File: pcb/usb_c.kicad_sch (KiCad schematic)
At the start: 6 parts, among them J5 USB_C_Receptacle_USB2.0_14P, U8 TPS2051CDBV, U9 USBLC6-2SC6

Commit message: pcb: satisfy ERC warnings and errors
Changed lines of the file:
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@@
+	)
+	(junction
+		(at 35.56 111.76)
+		(diameter 0)
+		(color 0 0 0 0)
 	)
 	(junction
@@
 	(wire
 		(pts
-			(xy 31.75 111.76) (xy 41.91 111.76)
+			(xy 31.75 111.76) (xy 35.56 111.76)
 		)
 		(stroke
@@
 		(pts
 			(xy 180.34 110.49) (xy 124.46 110.49)
+		)
+		(stroke
+			(width 0)
+			(type default)
+		)
+	)
+	(wire
+		(pts
+			(xy 35.56 111.76) (xy 41.91 111.76)
 		)
 		(stroke
@@
 					(unit 1)
 				)
+			)
+		)
+	)
+	(symbol
+		(lib_id "power:PWR_FLAG")
+		(at 35.56 111.76 0)
+		(unit 1)
+		(body_style 1)
+		(exclude_from_sim no)
+		(in_bom yes)
+		(on_board yes)
+		(in_pos_files yes)
+		(dnp no)
+		(fields_autoplaced yes)
+		(property "Reference" "#FLG05"
+			(at 35.56 109.855 0)
+			(hide yes)
+			(show_name no)
+			(do_not_autoplace no)
+			(effects
+				(font
+					(size 1.27 1.27)
+				)
+			)
+		)
+		(property "Value" "PWR_FLAG"
+			(at 35.56 106.68 0)
+			(show_name no)
+			(do_not_autoplace no)
+			(effects
+				(font
+					(size 1.27 1.27)
+				)
+			)
+		)
+		(property "Footprint" ""
+			(at 35.56 111.76 0)
+			(hide yes)
+			(show_name no)
+			(do_not_autoplace no)
+			(effects
+				(font
+					(size 1.27 1.27)
+				)
+			)
+		)
+		(property "Datasheet" ""
+			(at 35.56 111.76 0)
+			(hide yes)
+			(show_name no)
+			(do_not_autoplace no)
+			(effects
+				(font
+					(size 1.27 1.27)
+				)
+			)
+		)
+		(property "Description" "Special symbol for telling ERC where power comes from"
+			(at 35.56 111.76 0)
+			(hide yes)
+			(show_name no)
+			(do_not_autoplace no)
+			(effects
+				(font
+					(size 1.27 1.27)
+				)
+			)
+		)
+		(pin "1"
+		)
+		(instances
+			(project "tdt4295"
+				(path "/603dd496-f9c4-4a31-9104-19eec41ebc98/59405b24-6536-4799-b908-ee0def989f5c/ffd64d7a-b064-4a59-840d-09058194ff51"
+					(reference "#FLG05")
+					(unit 1)
+				)

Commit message: layout prep
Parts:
- removed J5: USB_C_Receptacle_USB2.0_14P, symbol Connector:USB_C_Receptacle_USB2.0_14P
- added J6: USB4110-GF-A, USB4110_GF_A:USB4110-GF-A_GCT, symbol USB4110_GF_A:USB4110-GF-A
- C72: footprint (none) -> Capacitor_SMD:C_0805_2012Metric_Pad1.18x1.45mm_HandSolder
- C73: footprint Package_TO_SOT_SMD:SOT-23-6 -> Capacitor_SMD:C_0805_2012Metric_Pad1.18x1.45mm_HandSolder
- R39: footprint (none) -> Resistor_SMD:R_0805_2012Metric_Pad1.20x1.40mm_HandSolder
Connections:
- net CC1: now also J6.A5 (CC1)
- net CC2: now also J6.B5 (CC2)
- net GND: now also J6.A1-B12 (GND), J6.A12-B1 (GND), J6.A8 (SBU1), J6.B8 (SBU2)
- net at C73.1, U8.1 (OUT): now also J6.A4-B9 (VBUS), J6.A9-B4 (VBUS)
- net at U9.1 (I/O1): now also J6.A6 (DP1), J6.B6 (DP2)
- net at U9.3 (I/O2): now also J6.A7 (DN1), J6.B7 (DN2)

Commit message: updates labels
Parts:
- renumbered C72 to C75, C73 to C76, R39 to R55
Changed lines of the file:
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@@
 		(dnp no)
 		(fields_autoplaced yes)
-		(property "Reference" "C72"
+		(property "Reference" "C75"
 			(at 49.53 125.7299 0)
 			(show_name no)
@@
 			(project "tdt4295"
 				(path "/603dd496-f9c4-4a31-9104-19eec41ebc98/59405b24-6536-4799-b908-ee0def989f5c/ffd64d7a-b064-4a59-840d-09058194ff51"
-					(reference "C72")
+					(reference "C75")
 					(unit 1)
 				)
@@
 		(dnp no)
 		(fields_autoplaced yes)
-		(property "Reference" "R39"
+		(property "Reference" "R55"
 			(at 44.45 99.0599 0)
 			(show_name no)
@@
 			(project "tdt4295"
 				(path "/603dd496-f9c4-4a31-9104-19eec41ebc98/59405b24-6536-4799-b908-ee0def989f5c/ffd64d7a-b064-4a59-840d-09058194ff51"
-					(reference "R39")
+					(reference "R55")
 					(unit 1)
 				)
@@
 		(dnp no)
 		(fields_autoplaced yes)
-		(property "Reference" "#PWR074"
+		(property "Reference" "#PWR077"
 			(at 45.72 137.16 0)
 			(hide yes)
@@
 			(project "tdt4295"
 				(path "/603dd496-f9c4-4a31-9104-19eec41ebc98/59405b24-6536-4799-b908-ee0def989f5c/ffd64d7a-b064-4a59-840d-09058194ff51"
-					(reference "#PWR074")
+					(reference "#PWR077")
 					(unit 1)
 				)
@@
 		(dnp no)
 		(fields_autoplaced yes)
-		(property "Reference" "#PWR075"
+		(property "Reference" "#PWR078"
 			(at 60.96 128.27 0)
 			(hide yes)
@@
 			(project "tdt4295"
 				(path "/603dd496-f9c4-4a31-9104-19eec41ebc98/59405b24-6536-4799-b908-ee0def989f5c/ffd64d7a-b064-4a59-840d-09058194ff51"
-					(reference "#PWR075")
+					(reference "#PWR078")
 					(unit 1)
 				)
@@
 		(dnp no)
 		(fields_autoplaced yes)
-		(property "Reference" "#PWR077"
+		(property "Reference" "#PWR080"
 			(at 180.34 120.65 0)
 			(hide yes)
@@
 			(project "tdt4295"
 				(path "/603dd496-f9c4-4a31-9104-19eec41ebc98/59405b24-6536-4799-b908-ee0def989f5c/ffd64d7a-b064-4a59-840d-09058194ff51"
-					(reference "#PWR077")
+					(reference "#PWR080")
 					(unit 1)
 				)
@@
 		(dnp no)
 		(fields_autoplaced yes)
-		(property "Reference" "#PWR076"
+		(property "Reference" "#PWR079"
 			(at 82.55 95.25 0)
 			(hide yes)
@@
 			(project "tdt4295"
 				(path "/603dd496-f9c4-4a31-9104-19eec41ebc98/59405b24-6536-4799-b908-ee0def989f5c/ffd64d7a-b064-4a59-840d-09058194ff51"
-					(reference "#PWR076")
+					(reference "#PWR079")
 					(unit 1)
 				)
@@
 		(dnp no)
 		(fields_autoplaced yes)
-		(property "Reference" "C73"
+		(property "Reference" "C76"
 			(at 86.36 103.8859 0)
 			(show_name no)
@@
 			(project "tdt4295"
 				(path "/603dd496-f9c4-4a31-9104-19eec41ebc98/59405b24-6536-4799-b908-ee0def989f5c/ffd64d7a-b064-4a59-840d-09058194ff51"
-					(reference "C73")
+					(reference "C76")
 					(unit 1)
 				)
@@
 		(dnp no)
 		(fields_autoplaced yes)
-		(property "Reference" "#FLG05"
+		(property "Reference" "#FLG06"
 			(at 35.56 109.855 0)
 			(hide yes)
@@
 			(project "tdt4295"
 				(path "/603dd496-f9c4-4a31-9104-19eec41ebc98/59405b24-6536-4799-b908-ee0def989f5c/ffd64d7a-b064-4a59-840d-09058194ff51"
-					(reference "#FLG05")
-					(unit 1)
-				)
+					(reference "#FLG06")
+					(unit 1)
+				)

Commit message: pcb: finalize erc
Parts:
- J6: footprint USB4110_GF_A:USB4110-GF-A_GCT -> USB4110-GF-A_GCT
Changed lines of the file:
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@@
 	(wire
 		(pts
-			(xy 215.9 110.49) (xy 187.96 110.49)
+			(xy 187.96 110.49) (xy 215.9 110.49)
 		)
 		(stroke
@@
 		)
 		(property "Extra" "5V"
-			(at 32.512 115.062 0)
+			(at 25.4 108.458 0)
 			(show_name no)
 			(do_not_autoplace no)
@@
 	)
 	(symbol
+		(lib_id "power:GND")
+		(at 180.34 114.3 0)
+		(unit 1)
+		(body_style 1)
+		(exclude_from_sim no)
+		(in_bom yes)
+		(on_board yes)
+		(in_pos_files yes)
+		(dnp no)
+		(fields_autoplaced yes)
+		(property "Reference" "#PWR080"
+			(at 180.34 120.65 0)
+			(hide yes)
+			(show_name no)
+			(do_not_autoplace no)
+			(effects
+				(font
+					(size 1.27 1.27)
+				)
+			)
+		)
+		(property "Value" "GND"
+			(at 180.34 119.38 0)
+			(show_name no)
+			(do_not_autoplace no)
+			(effects
+				(font
+					(size 1.27 1.27)
+				)
+			)
+		)
+		(property "Footprint" ""
+			(at 180.34 114.3 0)
+			(hide yes)
+			(show_name no)
+			(do_not_autoplace no)
+			(effects
+				(font
+					(size 1.27 1.27)
+				)
+			)
+		)
+		(property "Datasheet" ""
+			(at 180.34 114.3 0)
+			(hide yes)
+			(show_name no)
+			(do_not_autoplace no)
+			(effects
+				(font
+					(size 1.27 1.27)
+				)
+			)
+		)
+		(property "Description" "Power symbol creates a global label with name \"GND\" , ground"
+			(at 180.34 114.3 0)
+			(hide yes)
+			(show_name no)
+			(do_not_autoplace no)
+			(effects
+				(font
+					(size 1.27 1.27)
+				)
+			)
+		)
+		(pin "1"
+		)
+		(instances
+			(project "tdt4295"
+				(path "/603dd496-f9c4-4a31-9104-19eec41ebc98/59405b24-6536-4799-b908-ee0def989f5c/ffd64d7a-b064-4a59-840d-09058194ff51"
+					(reference "#PWR080")
+					(unit 1)
+				)
+			)
+		)
+	)
+	(symbol
 		(lib_id "Device:C")
 		(at 45.72 127 0)
@@
 			)
 		)
-		(property "Footprint" "USB4110_GF_A:USB4110-GF-A_GCT"
+		(property "Footprint" "USB4110-GF-A_GCT"
 			(at 215.9 92.71 0)
 			(hide yes)
@@
 					(unit 1)
 				)
-			)
-		)
-	)
-	(symbol
-		(lib_id "power:GND")
-		(at 180.34 114.3 0)
-		(unit 1)
-		(body_style 1)
-		(exclude_from_sim no)
-		(in_bom yes)
-		(on_board yes)
-		(in_pos_files yes)
-		(dnp no)
-		(fields_autoplaced yes)
-		(property "Reference" "#PWR080"
-			(at 180.34 120.65 0)
-			(hide yes)
-			(show_name no)
-			(do_not_autoplace no)
-			(effects
-				(font
-					(size 1.27 1.27)
-				)
-			)
-		)
-		(property "Value" "GND"
-			(at 180.34 119.38 0)
-			(show_name no)
-			(do_not_autoplace no)
-			(effects
-				(font
-					(size 1.27 1.27)
-				)
-			)
-		)
-		(property "Footprint" ""
-			(at 180.34 114.3 0)
-			(hide yes)
-			(show_name no)
-			(do_not_autoplace no)
-			(effects
-				(font
-					(size 1.27 1.27)
-				)
-			)
-		)
-		(property "Datasheet" ""
-			(at 180.34 114.3 0)
-			(hide yes)
-			(show_name no)
-			(do_not_autoplace no)
-			(effects
-				(font
-					(size 1.27 1.27)
-				)
-			)
-		)
-		(property "Description" "Power symbol creates a global label with name \"GND\" , ground"
-			(at 180.34 114.3 0)
-			(hide yes)
-			(show_name no)
-			(do_not_autoplace no)
-			(effects
-				(font
-					(size 1.27 1.27)
-				)
-			)
-		)
-		(pin "1"
-		)
-		(instances
-			(project "tdt4295"
-				(path "/603dd496-f9c4-4a31-9104-19eec41ebc98/59405b24-6536-4799-b908-ee0def989f5c/ffd64d7a-b064-4a59-840d-09058194ff51"
-					(reference "#PWR080")
-					(unit 1)
-				)

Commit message: pcb: pds rough placement
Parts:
- J6: footprint USB4110-GF-A_GCT -> USB4110_GF_A:USB4110-GF-A_GCT
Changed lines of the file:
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@@
 			)
 		)
-		(property "Footprint" "USB4110-GF-A_GCT"
+		(property "Footprint" "USB4110_GF_A:USB4110-GF-A_GCT"
 			(at 215.9 92.71 0)
 			(hide yes)

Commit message: pcb: address feedback
- make rgb565 resistor ladder
- add 1v0 diode
- clean up pwr flags
- remove unused mcu-sd spi
- use labels in mcu
- fix broken rgb diode
- connect usblc pin 5 to vbus
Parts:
- renumbered R55 to R56
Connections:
- net at C76.1, J6.A4-B9 (VBUS), J6.A9-B4 (VBUS)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: now also U9.5 (VBUS)
- no-connect marks 1 -> 0
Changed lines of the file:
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@@
-	)
-	(junction
-		(at 35.56 111.76)
-		(diameter 0)
-		(color 0 0 0 0)
 	)
 	(junction
@@
 	)
 	(junction
+		(at 124.46 72.39)
+		(diameter 0)
+		(color 0 0 0 0)
+	)
+	(junction
 		(at 172.72 110.49)
 		(diameter 0)
@@
 		(color 0 0 0 0)
 	)
-	(no_connect
-		(at 124.46 81.28)
-	)
 	(wire
 		(pts
@@
 	(wire
 		(pts
+			(xy 124.46 72.39) (xy 175.26 72.39)
+		)
+		(stroke
+			(width 0)
+			(type default)
+		)
+	)
+	(wire
+		(pts
 			(xy 180.34 110.49) (xy 180.34 114.3)
 		)
@@
 	(wire
 		(pts
-			(xy 31.75 111.76) (xy 35.56 111.76)
-		)
-		(stroke
-			(width 0)
-			(type default)
-		)
-	)
-	(wire
-		(pts
 			(xy 74.93 96.52) (xy 74.93 116.84)
 		)
@@
 	(wire
 		(pts
-			(xy 35.56 111.76) (xy 41.91 111.76)
+			(xy 31.75 111.76) (xy 41.91 111.76)
 		)
 		(stroke
@@
 	(wire
 		(pts
-			(xy 97.79 72.39) (xy 175.26 72.39)
+			(xy 124.46 72.39) (xy 124.46 81.28)
+		)
+		(stroke
+			(width 0)
+			(type default)
+		)
+	)
+	(wire
+		(pts
+			(xy 97.79 72.39) (xy 124.46 72.39)
 		)
 		(stroke
@@
 		(dnp no)
 		(fields_autoplaced yes)
-		(property "Reference" "#PWR080"
+		(property "Reference" "#PWR082"
 			(at 180.34 120.65 0)
 			(hide yes)
@@
 			(project "tdt4295"
 				(path "/603dd496-f9c4-4a31-9104-19eec41ebc98/59405b24-6536-4799-b908-ee0def989f5c/ffd64d7a-b064-4a59-840d-09058194ff51"
-					(reference "#PWR080")
+					(reference "#PWR082")
 					(unit 1)
 				)
@@
 		(dnp no)
 		(fields_autoplaced yes)
-		(property "Reference" "R55"
+		(property "Reference" "R56"
 			(at 44.45 99.0599 0)
 			(show_name no)
@@
 			(project "tdt4295"
 				(path "/603dd496-f9c4-4a31-9104-19eec41ebc98/59405b24-6536-4799-b908-ee0def989f5c/ffd64d7a-b064-4a59-840d-09058194ff51"
-					(reference "R55")
+					(reference "R56")
 					(unit 1)
 				)
@@
 		(dnp no)
 		(fields_autoplaced yes)
-		(property "Reference" "#PWR077"
+		(property "Reference" "#PWR079"
 			(at 45.72 137.16 0)
 			(hide yes)
@@
 			(project "tdt4295"
 				(path "/603dd496-f9c4-4a31-9104-19eec41ebc98/59405b24-6536-4799-b908-ee0def989f5c/ffd64d7a-b064-4a59-840d-09058194ff51"
-					(reference "#PWR077")
+					(reference "#PWR079")
 					(unit 1)
 				)
@@
 		(dnp no)
 		(fields_autoplaced yes)
-		(property "Reference" "#PWR078"
+		(property "Reference" "#PWR080"
 			(at 60.96 128.27 0)
 			(hide yes)
@@
 			(project "tdt4295"
 				(path "/603dd496-f9c4-4a31-9104-19eec41ebc98/59405b24-6536-4799-b908-ee0def989f5c/ffd64d7a-b064-4a59-840d-09058194ff51"
-					(reference "#PWR078")
+					(reference "#PWR080")
 					(unit 1)
 				)
@@
 		(dnp no)
 		(fields_autoplaced yes)
-		(property "Reference" "#PWR079"
+		(property "Reference" "#PWR081"
 			(at 82.55 95.25 0)
 			(hide yes)
@@
 			(project "tdt4295"
 				(path "/603dd496-f9c4-4a31-9104-19eec41ebc98/59405b24-6536-4799-b908-ee0def989f5c/ffd64d7a-b064-4a59-840d-09058194ff51"
-					(reference "#PWR079")
+					(reference "#PWR081")
 					(unit 1)
 				)
@@
 					(unit 1)
 				)
-			)
-		)
-	)
-	(symbol
-		(lib_id "power:PWR_FLAG")
-		(at 35.56 111.76 0)
-		(unit 1)
-		(body_style 1)
-		(exclude_from_sim no)
-		(in_bom yes)
-		(on_board yes)
-		(in_pos_files yes)
-		(dnp no)
-		(fields_autoplaced yes)
-		(property "Reference" "#FLG06"
-			(at 35.56 109.855 0)
-			(hide yes)
-			(show_name no)
-			(do_not_autoplace no)
-			(effects
-				(font
-					(size 1.27 1.27)
-				)
-			)
-		)
-		(property "Value" "PWR_FLAG"
-			(at 35.56 106.68 0)
-			(show_name no)
-			(do_not_autoplace no)
-			(effects
-				(font
-					(size 1.27 1.27)
-				)
-			)
-		)
-		(property "Footprint" ""
-			(at 35.56 111.76 0)
-			(hide yes)
-			(show_name no)
-			(do_not_autoplace no)
-			(effects
-				(font
-					(size 1.27 1.27)
-				)
-			)
-		)
-		(property "Datasheet" ""
-			(at 35.56 111.76 0)
-			(hide yes)
-			(show_name no)
-			(do_not_autoplace no)
-			(effects
-				(font
-					(size 1.27 1.27)
-				)
-			)
-		)
-		(property "Description" "Special symbol for telling ERC where power comes from"
-			(at 35.56 111.76 0)
-			(hide yes)
-			(show_name no)
-			(do_not_autoplace no)
-			(effects
-				(font
-					(size 1.27 1.27)
-				)
-			)
-		)
-		(pin "1"
-		)
-		(instances
-			(project "tdt4295"
-				(path "/603dd496-f9c4-4a31-9104-19eec41ebc98/59405b24-6536-4799-b908-ee0def989f5c/ffd64d7a-b064-4a59-840d-09058194ff51"
-					(reference "#FLG06")
-					(unit 1)
-				)

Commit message: pcb
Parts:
- renumbered C75 to C69, C76 to C70, J6 to J7, R56 to R60, U8 to U7, U9 to U8

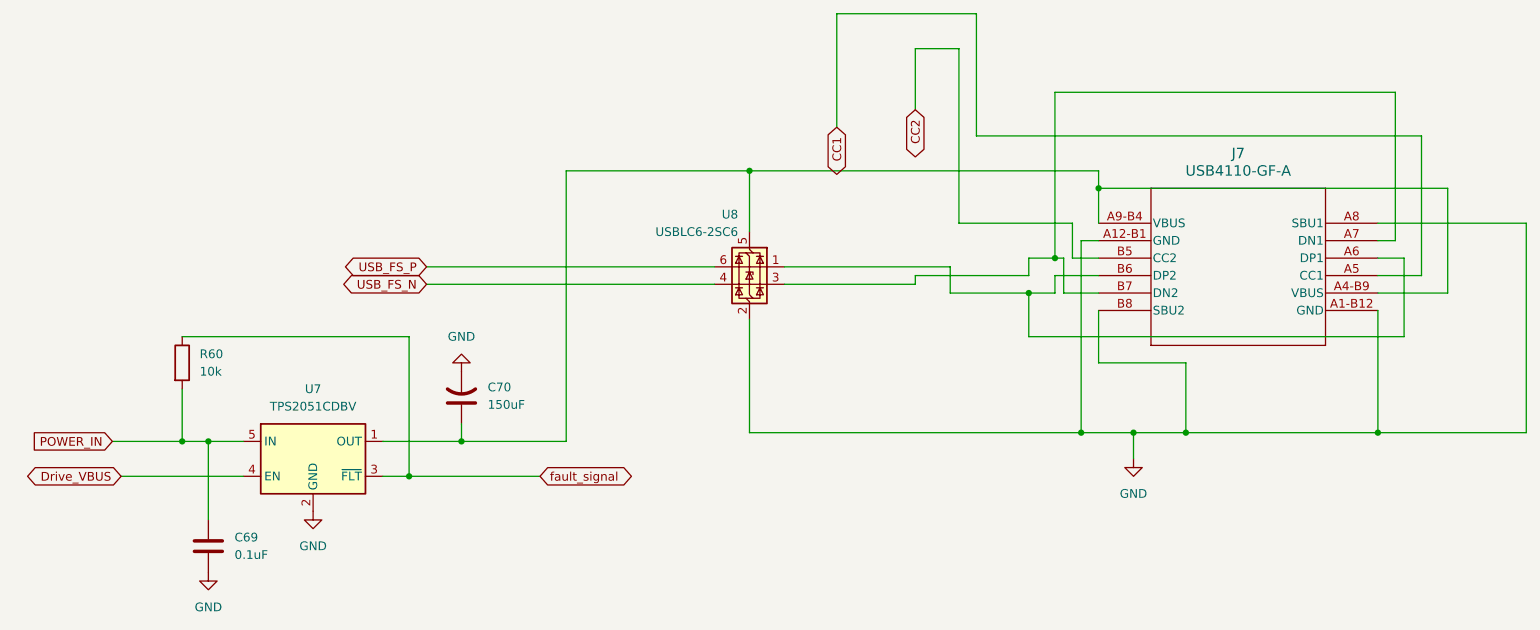
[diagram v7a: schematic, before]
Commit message: fix usb symbol
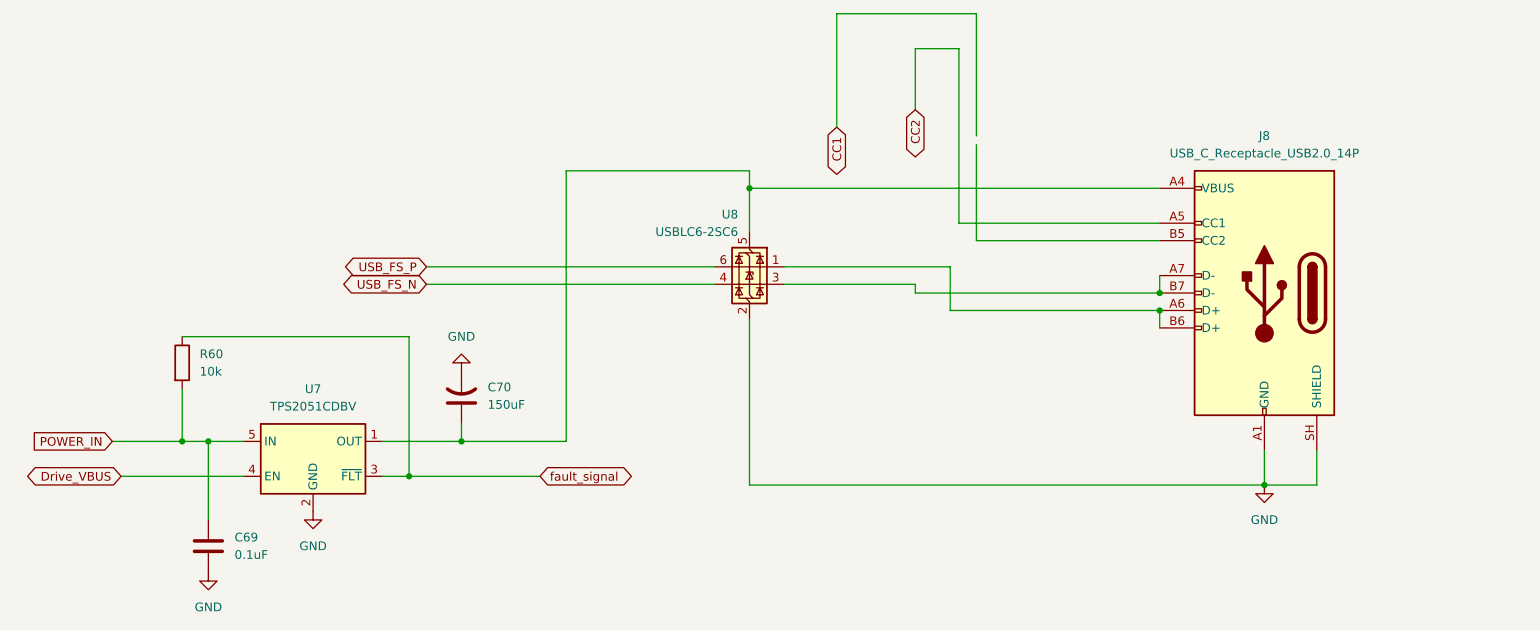
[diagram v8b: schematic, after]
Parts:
- removed J7: USB4110-GF-A, USB4110_GF_A:USB4110-GF-A_GCT, symbol USB4110_GF_A:USB4110-GF-A
- added J8: USB_C_Receptacle_USB2.0_14P, USB4110_GF_A:USB4110-GF-A_GCT, symbol Connector:USB_C_Receptacle_USB2.0_14P
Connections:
- net CC2: now also J8.A5 (CC1)
- net GND: now also J8.A1 (GND), J8.A12 (GND), J8.B1 (GND), J8.B12 (GND), J8.SH (SHIELD)
- net at C70.1, U7.1 (OUT), U8.5 (VBUS): now also J8.A4 (VBUS), J8.A9 (VBUS), J8.B4 (VBUS), J8.B9 (VBUS)
- net at U8.1 (I/O1): now also J8.A6 (D+), J8.B6 (D+)
- net at U8.3 (I/O2): now also J8.A7 (D-), J8.B7 (D-)
